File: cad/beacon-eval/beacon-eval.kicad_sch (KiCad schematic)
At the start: 18 parts, among them J1 XNANO_J200, J2 BENCH_5V_3A, J3 LED_CARRIER, U1 LM3410XMF-NOPB, U3 TPS3839L30DBVT

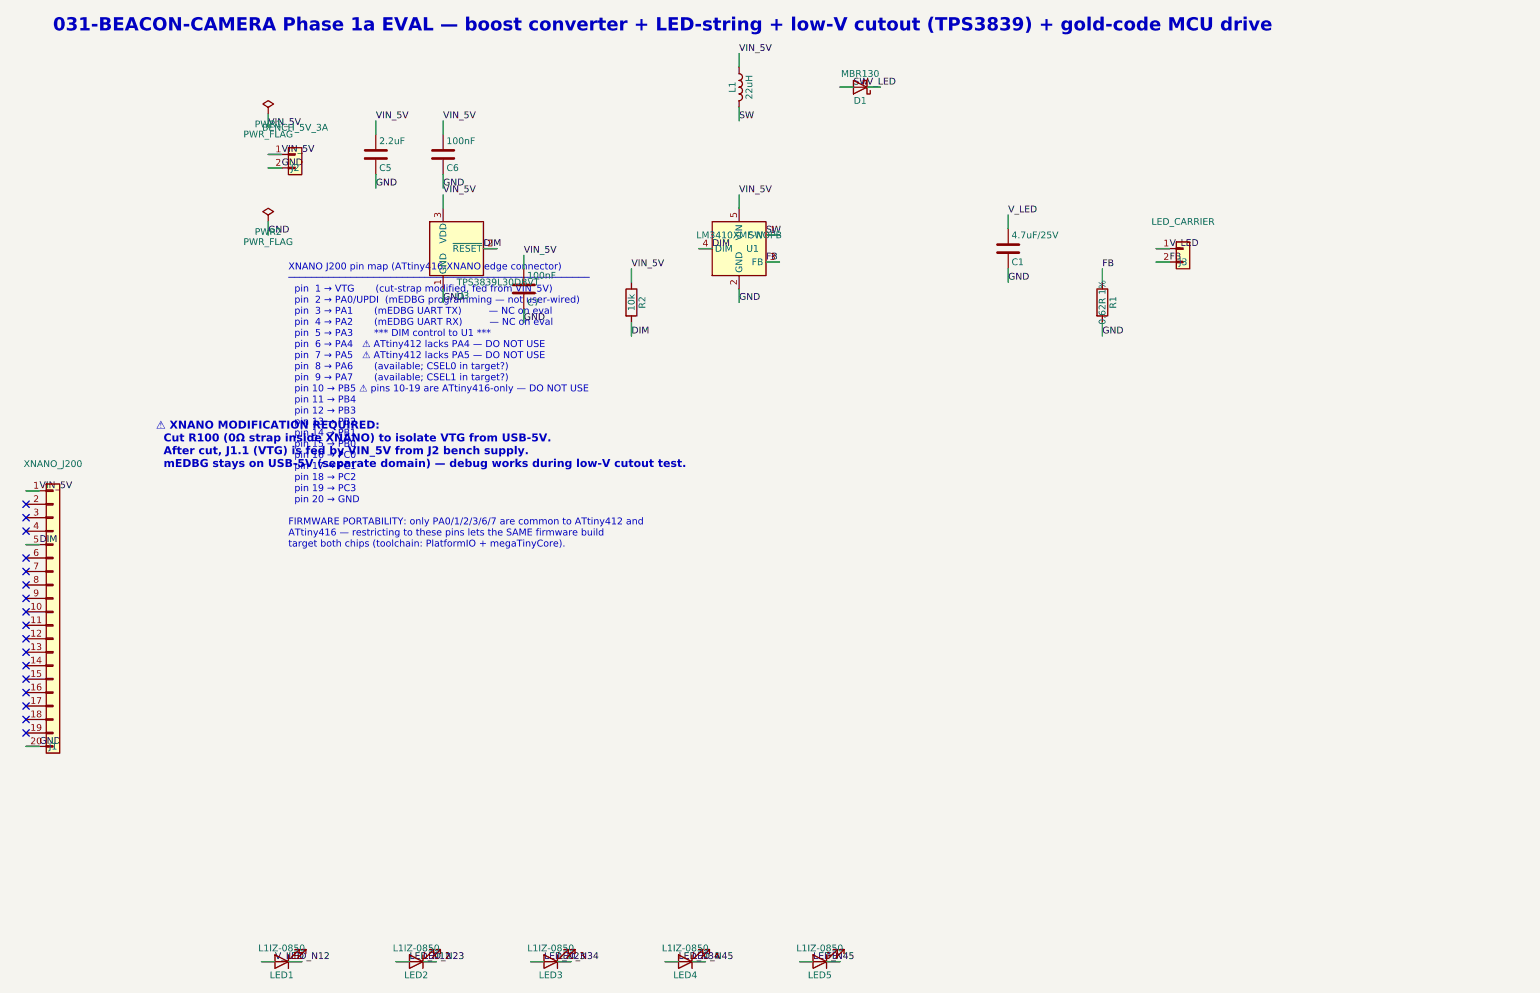
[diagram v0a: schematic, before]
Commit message: feat(031 phase 1a): beacon-eval schematic — apply R11 + add JST-PH battery input
Hand-editing pass in eeschema completes the schematic-side cascade of R11
(commit 121f5ba landed the spec/plan/research/BOM updates). Plus operator
asked to add back a 2-pin power input header matching the flight battery's
JST-PH 2.0 mm pigtail.

R11 topology changes:
  - U3 (TPS3839 supervisor IC) DELETED
  - C7 (supervisor decoupling cap) DELETED
  - R2 (10 kOhm DIM resistor) reversed: was pull-UP to V_BAT, now pull-DOWN
    to GND (topological failsafe — MCU PA3 high-Z -> DIM LOW -> LEDs OFF)
  - DIM net now has exactly two drivers: U1.DIM (boost shutdown control)
    and J1.5 (XNANO PA3, MCU push-pull active-HIGH); no more wired-AND

Layout pass:
  - Component spacing increased (boost cluster previously jammed into
    ~20x20 mm now spread across page width)
  - LED string LED1..LED5 moved up next to D1 / C1, chained left-to-right
    after 180 deg rotation (anode-left, cathode-right)
  - LED-carrier connector J3 removed — LED string is wired on-page
  - All five LEDs rotated 180 deg for clean L->R series chain
  - D1 rotated 180 deg (anode on SW side, cathode on V_LED side; current
    flows L->R visually through the boost stage)

Power input (new this pass):
  - J2 (Conn_01x02, JST-PH 2.0 mm horizontal socket) added — mates with
    the flight battery's standard JST-PH 2-pin pigtail. Pin 1 = VIN_5V,
    pin 2 = GND. Same socket footprint as the target-pod battery
    connector, so the eval validates the actual battery-to-pod
    insertion path (battery-as-switch per FR-1.2).
  - On the eval, J2 also accepts a bench-supply harness in place of the
    battery, for controlled VIN ramps during the firmware-ADC cutoff test.
  - PWR1 + PWR2 PWR_FLAGs added on VIN_5V and GND respectively — declares
    these nets as externally driven (J2 passive connector pins alone
    don't satisfy ERC's "input power pin not driven" check).
  - PWR1/J2/PWR2 organized as a tidy vertical column in the to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
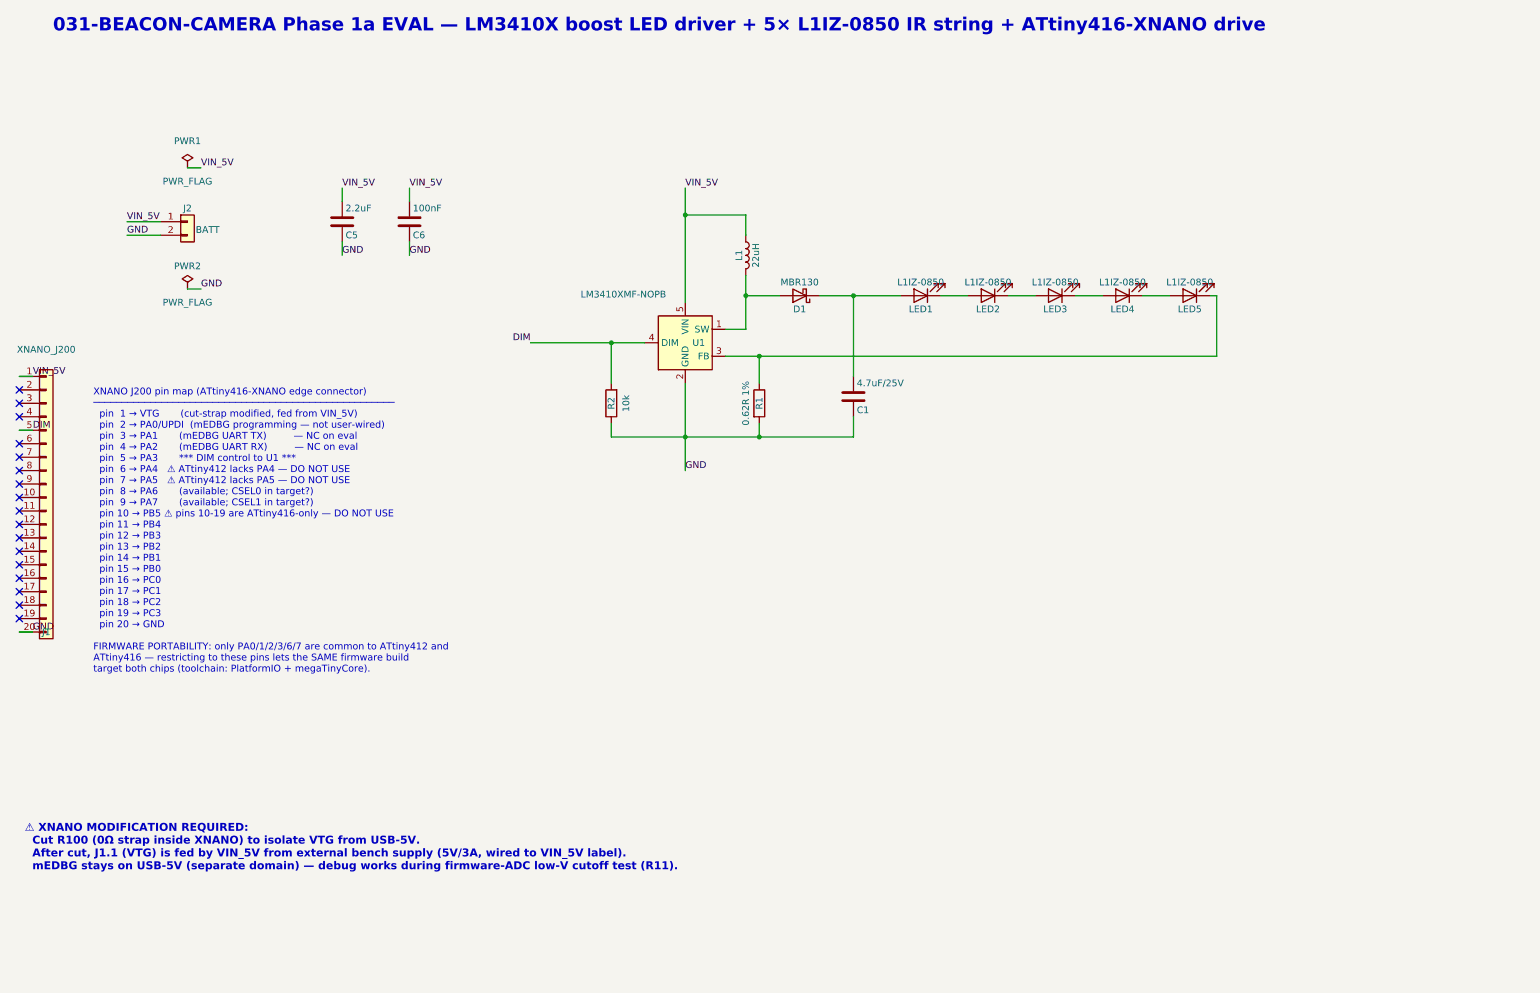
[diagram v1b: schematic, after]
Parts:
- removed C7: 100nF, Capacitor_SMD:C_0603_1608Metric, symbol Device:C
- removed J3: LED_CARRIER, Connector_PinHeader_2.54mm:PinHeader_1x02_P2.54mm_Vertical, symbol Connector_Generic:Conn_01x02
- removed U3: TPS3839L30DBVT, Package_TO_SOT_SMD:SOT-23-5, symbol Power_Supervisor:TPS3839DBZ
- J2: value BENCH_5V_3A -> BATT; footprint TerminalBlock:TerminalBlock_bornier-2_P5.08mm -> Connector_JST:JST_PH_S2B-PH-K-S_1x02_P2.00mm_Horizontal
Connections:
- net GND: now also R2.1
- net VIN_5V: no longer R2.1
- net FB: no longer names the net of LED5.1 (K), R1.1, U1.3 (FB)
- net LED_N12: no longer names the net of LED1.1 (K), LED2.2 (A)
- net LED_N23: no longer names the net of LED2.1 (K), LED3.2 (A)
- net LED_N34: no longer names the net of LED3.1 (K), LED4.2 (A)
- net LED_N45: no longer names the net of LED4.1 (K), LED5.2 (A)
- net SW: no longer names the net of D1.2 (A), L1.2, U1.1 (SW)
- net V_LED: no longer names the net of C1.1, D1.1 (K), LED1.2 (A)
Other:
- note added: "031-BEACON-CAMERA Phase 1a EVAL — LM3410X boost LED driver + 5× L1IZ-0850 IR string + ATtiny416-XNANO drive"
- note added: "⚠ XNANO MODIFICATION REQUIRED: Cut R100 (0Ω strap inside XNANO) to isolate VTG from USB-5V. After cut, J1.1 (VTG) is fed by VIN_5V from external bench supply (5V/3A, wired to VIN_5V label). mEDBG stays on USB-5V (separate domain) — debug works during firmware-ADC low-V cutoff test (R11)."
- note removed: "031-BEACON-CAMERA Phase 1a EVAL — boost converter + LED-string + low-V cutout (TPS3839) + gold-code MCU drive"
- note removed: "⚠ XNANO MODIFICATION REQUIRED: Cut R100 (0Ω strap inside XNANO) to isolate VTG from USB-5V. After cut, J1.1 (VTG) is fed by VIN_5V from J2 bench supply. mEDBG stays on USB-5V (separate domain) — debug works during low-V cutout test."
- moved on the sheet: C1, C5, C6, D1, J1, L1, LED1, LED2, LED3, LED4, LED5, R1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

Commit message: feat(031): beacon-eval order-02 + BOM tweaks; backlog OG0VA inquiry + code-sync study
Beacon-eval schematic/BOM adjustments and a second order sheet (beacon-order-02).
Two new 031 backlog items: OG0VA design-house register-spec/eval-module inquiry
(deferred while designing on the paper product brief), and a study on code-derived
shutter sync + sub-100% chip-on pulsing for lower emitter power / better RC-osc
stability.

Co-Authored-By: Claude Opus 4.8 (1M context) <noreply@anthropic.com>
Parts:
- R1: value 0.62R 1% -> 3.74R 1%
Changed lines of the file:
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@@
 			)
 		)
-		(property "Value" "0.62R 1%"
+		(property "Value" "3.74R 1%"
 			(at 166.37 82.55 90)
 			(show_name no)

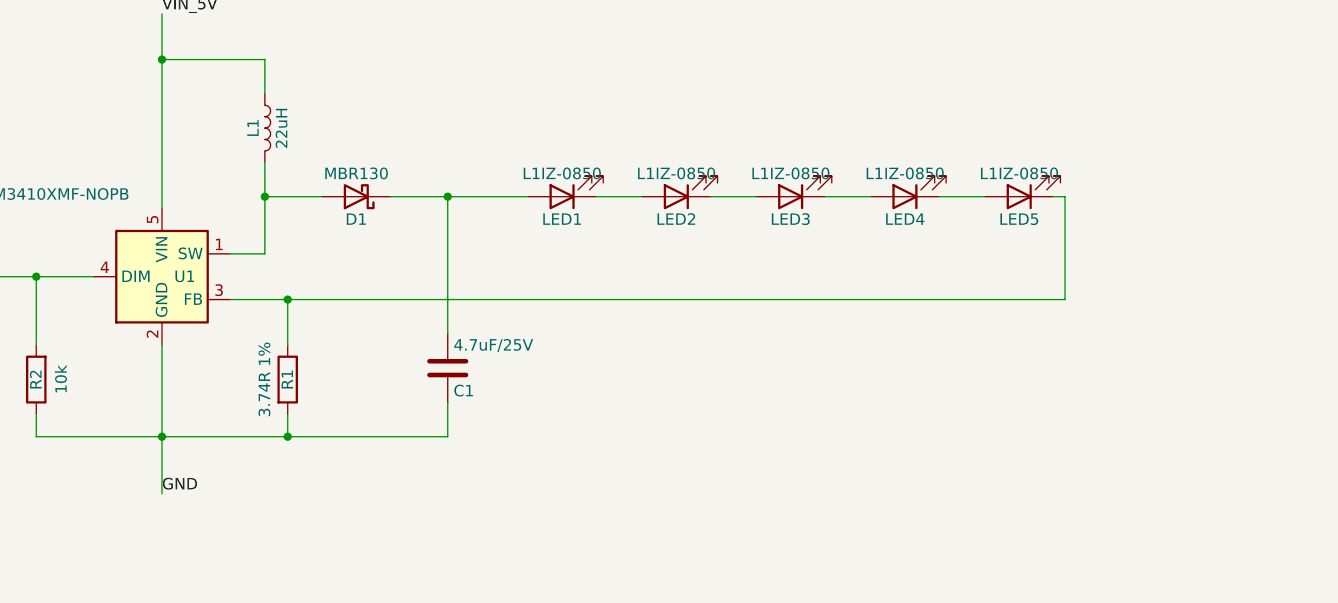
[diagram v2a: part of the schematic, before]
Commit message: cad(031): emitter schematic OVP clamp verified + PDF regenerated (wrap item 1)
D2 15 V zener cathode->V_OUT (LED-string anode rail) / anode->FB; R3 1k
in series FB->sense node (top of R1) -- matches the TI OVP recipe and the
BOM's EV-A13/A14 (BOM refdes D3/R4 = sheet D2/R3). Verified on the
rendered PDF (a symbol-rotation read had wrongly flagged it reversed --
the drawing is ground truth). Bench sheet; flight deltas tabled in
verified-bom-eval.md.

Co-Authored-By: Claude Fable 5 <noreply@anthropic.com>
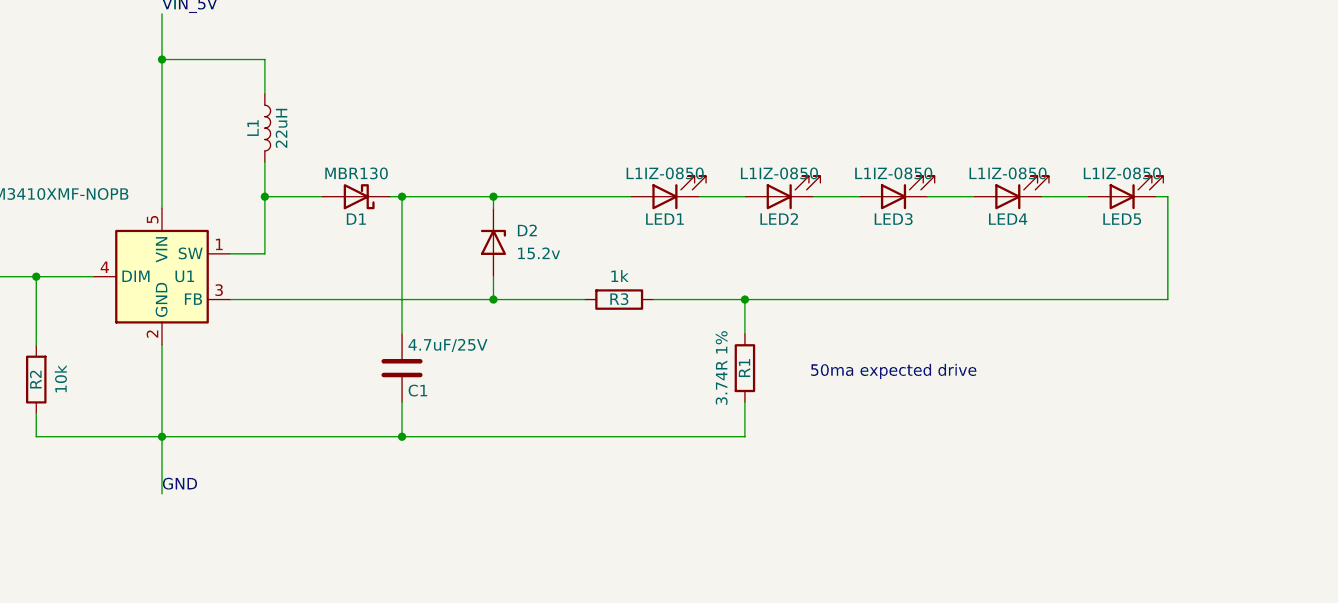
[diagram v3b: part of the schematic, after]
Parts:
- added D2: 15.2v, symbol Device:D_Zener
- added R3: 1k, Resistor_SMD:R_1206_3216Metric, symbol Device:R
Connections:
- net at C1.1, D1.1 (K), LED1.2 (A): now also D2.1 (K)
- net at LED5.1 (K), R1.1: now also R3.1; no longer U1.3 (FB)
- new net: D2.2 (A), R3.2, U1.3 (FB)
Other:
- note added: "50ma expected drive"
- moved on the sheet: C1, LED1, LED2, LED3, LED4, LED5, R1

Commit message: cad(031): D1 is SS1030 on bench AND flight (MBR130 = stale original spec, never bought); sheet value + table fixed
Co-Authored-By: Claude Fable 5 <noreply@anthropic.com>
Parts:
- D1: value MBR130 -> SS1030
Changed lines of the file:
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@@
 			)
 		)
-		(property "Value" "MBR130"
+		(property "Value" "SS1030"
 			(at 176.53 59.69 0)
 			(show_name no)

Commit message: cad(031): eval sheet -- bench/flight value table on-sheet, L1/R1 'See table', D1=SS1030; PDF regenerated
Operator added the Device/Bench/Flight/Notes table (L1 22->4.7 uH, R1
3.74->0.62 R). Netlist re-verified (DIM/GND/VIN_5V + boost/OVP mesh);
rendered PDF checked for refs + orientation.

Co-Authored-By: Claude Fable 5 <noreply@anthropic.com>
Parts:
- L1: value 22uH -> See table
- R1: value 3.74R 1% -> See table
